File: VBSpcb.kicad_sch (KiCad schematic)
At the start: 14 parts, among them J1 Conn_01x03, J2 DB25_Receptacle, U1 LF356

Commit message: Updated Silkscreen
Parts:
- J1: value Conn_01x03 -> Video In
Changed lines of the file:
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@@
       (effects (font (size 1.27 1.27)) (justify left))
     )
-    (property "Value" "Conn_01x03" (at 45.72 81.28 0)
+    (property "Value" "Video In" (at 45.72 81.28 0)
       (effects (font (size 1.27 1.27)) (justify left))
     )

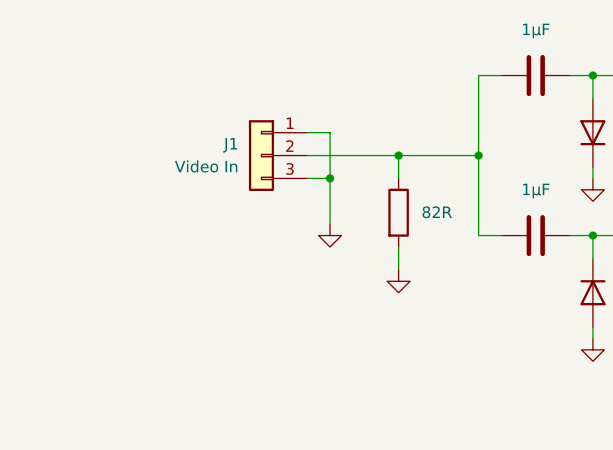
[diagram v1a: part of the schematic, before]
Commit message: Added nubbin for strain releif
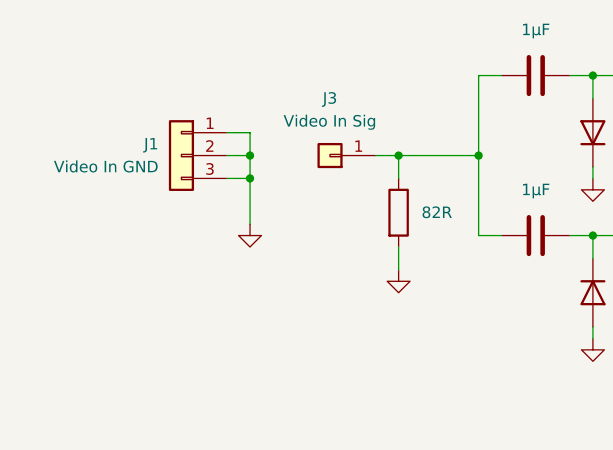
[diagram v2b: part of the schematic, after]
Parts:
- added J3: Video In Sig, Connector_PinHeader_2.54mm:PinHeader_1x01_P2.54mm_Vertical, symbol Connector_Generic:Conn_01x01
- J1: value Video In -> Video In GND
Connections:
- net GND: now also J1.2 (Pin_2)
- net at C1.1, C2.1, R1.1: now also J3.1 (Pin_1); no longer J1.2 (Pin_2)
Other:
- moved on the sheet: J1
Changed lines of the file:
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@@
   (junction (at 85.09 71.12) (diameter 0) (color 0 0 0 0)
   )
-  (junction (at 55.88 82.55) (diameter 0) (color 0 0 0 0)
+  (junction (at 63.5 80.01) (diameter 0) (color 0 0 0 0)
+  )
+  (junction (at 46.99 82.55) (diameter 0) (color 0 0 0 0)
   )
   (junction (at 72.39 80.01) (diameter 0) (color 0 0 0 0)
   )
-  (junction (at 63.5 80.01) (diameter 0) (color 0 0 0 0)
-  )
   (junction (at 142.24 115.57) (diameter 0) (color 0 0 0 0)
   )
@@
   (junction (at 127 82.55) (diameter 0) (color 0 0 0 0)
   )
+  (junction (at 46.99 80.01) (diameter 0) (color 0 0 0 0)
+  )
   (wire (pts (xy 99.06 71.12) (xy 99.06 80.01))
     (stroke (width 0) (type default))
@@
     (stroke (width 0) (type default))
   )
+  (wire (pts (xy 60.96 80.01) (xy 63.5 80.01))
+    (stroke (width 0) (type default))
+  )
   (wire (pts (xy 85.09 71.12) (xy 85.09 73.66))
     (stroke (width 0) (type default))
@@
     (stroke (width 0) (type default))
   )
-  (wire (pts (xy 53.34 77.47) (xy 55.88 77.47))
+  (wire (pts (xy 44.45 77.47) (xy 46.99 77.47))
     (stroke (width 0) (type default))
   )
@@
     (stroke (width 0) (type default))
   )
-  (wire (pts (xy 53.34 82.55) (xy 55.88 82.55))
+  (wire (pts (xy 44.45 82.55) (xy 46.99 82.55))
     (stroke (width 0) (type default))
   )
@@
     (stroke (width 0) (type default))
   )
-  (wire (pts (xy 55.88 82.55) (xy 55.88 87.63))
+  (wire (pts (xy 46.99 82.55) (xy 46.99 87.63))
     (stroke (width 0) (type default))
   )
@@
     (stroke (width 0) (type default))
   )
-  (wire (pts (xy 55.88 77.47) (xy 55.88 82.55))
+  (wire (pts (xy 46.99 77.47) (xy 46.99 80.01))
     (stroke (width 0) (type default))
   )
@@
     (stroke (width 0) (type default))
   )
+  (wire (pts (xy 46.99 80.01) (xy 46.99 82.55))
+    (stroke (width 0) (type default))
+  )
   (wire (pts (xy 96.52 71.12) (xy 99.06 71.12))
     (stroke (width 0) (type default))
@@
     (stroke (width 0) (type default))
   )
-  (wire (pts (xy 53.34 80.01) (xy 63.5 80.01))
-    (stroke (width 0) (type default))
-  )
   (wire (pts (xy 127 102.87) (xy 127 105.41))
     (stroke (width 0) (type default))
   )
   (wire (pts (xy 142.24 114.3) (xy 142.24 115.57))
+    (stroke (width 0) (type default))
+  )
+  (wire (pts (xy 44.45 80.01) (xy 46.99 80.01))
     (stroke (width 0) (type default))
   )
@@
     )
   )
-  (symbol (lib_id "power:GND") (at 55.88 87.63 0) (unit 1)
-    (in_bom yes) (on_board yes) (dnp no) (fields_autoplaced)
-    (property "Reference" "#PWR01" (at 55.88 93.98 0)
-      (effects (font (size 1.27 1.27)) hide)
-    )
-    (property "Value" "GND" (at 55.88 92.71 0)
-      (effects (font (size 1.27 1.27)) hide)
-    )
-    (property "Footprint" "" (at 55.88 87.63 0)
-      (effects (font (size 1.27 1.27)) hide)
-    )
-    (property "Datasheet" "" (at 55.88 87.63 0)
+  (symbol (lib_id "power:GND") (at 46.99 87.63 0) (unit 1)
+    (in_bom yes) (on_board yes) (dnp no) (fields_autoplaced)
+    (property "Reference" "#PWR01" (at 46.99 93.98 0)
+      (effects (font (size 1.27 1.27)) hide)
+    )
+    (property "Value" "GND" (at 46.99 92.71 0)
+      (effects (font (size 1.27 1.27)) hide)
+    )
+    (property "Footprint" "" (at 46.99 87.63 0)
+      (effects (font (size 1.27 1.27)) hide)
+    )
+    (property "Datasheet" "" (at 46.99 87.63 0)
       (effects (font (size 1.27 1.27)) hide)
     )
@@
         (path "/1a8ad53d-58ba-415b-ae19-54d4ebc887f3"
           (reference "#PWR01") (unit 1)
+        )
+      )
+    )
+  )
+  (symbol (lib_id "Connector_Generic:Conn_01x01") (at 55.88 80.01 180) (unit 1)
+    (in_bom yes) (on_board yes) (dnp no) (fields_autoplaced)
+    (property "Reference" "J3" (at 55.88 73.66 0)
+      (effects (font (size 1.27 1.27)))
+    )
+    (property "Value" "Video In Sig" (at 55.88 76.2 0)
+      (effects (font (size 1.27 1.27)))
+    )
+    (property "Footprint" "Connector_PinHeader_2.54mm:PinHeader_1x01_P2.54mm_Vertical" (at 55.88 80.01 0)
+      (effects (font (size 1.27 1.27)) hide)
+    )
+    (property "Datasheet" "~" (at 55.88 80.01 0)
+      (effects (font (size 1.27 1.27)) hide)
+    )
+    (pin "1")
+    (instances
+      (project "VBSpcb"
+        (path "/1a8ad53d-58ba-415b-ae19-54d4ebc887f3"
+          (reference "J3") (unit 1)
         )
       )
@@
     )
   )
-  (symbol (lib_id "Connector_Generic:Conn_01x03") (at 48.26 80.01 0) (mirror y) (unit 1)
+  (symbol (lib_id "Connector_Generic:Conn_01x03") (at 39.37 80.01 0) (mirror y) (unit 1)
     (in_bom yes) (on_board yes) (dnp no)
-    (property "Reference" "J1" (at 45.72 78.74 0)
-      (effects (font (size 1.27 1.27)) (justify left))
-    )
-    (property "Value" "Video In" (at 45.72 81.28 0)
-      (effects (font (size 1.27 1.27)) (justify left))
-    )
-    (property "Footprint" "Connector_PinHeader_2.54mm:PinHeader_1x03_P2.54mm_Vertical" (at 48.26 80.01 0)
-      (effects (font (size 1.27 1.27)) hide)
-    )
-    (property "Datasheet" "~" (at 48.26 80.01 0)
-      (effects (font (size 1.27 1.27)) hide)
-    )
+    (property "Reference" "J1" (at 36.83 78.74 0)
+      (effects (font (size 1.27 1.27)) (justify left))
+    )
+    (property "Value" "Video In GND" (at 36.83 81.28 0)
+      (effects (font (size 1.27 1.27)) (justify left))
+    )
+    (property "Footprint" "Connector_PinHeader_2.54mm:PinHeader_1x03_P2.54mm_Vertical" (at 39.37 80.01 0)
+      (effects (font (size 1.27 1.27)) hide)
+    )
+    (property "Datasheet" "~" (at 39.37 80.01 0)
+      (effects (font (size 1.27 1.27)) hide)
+    )
